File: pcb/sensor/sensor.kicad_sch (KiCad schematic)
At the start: 21 parts, among them J1 Conn_01x02_Pin, J2 Conn_01x02_Pin, J3 sig_in, J4 sig_out, J5 Conn_01x02_Pin, J6 Conn_01x02_Pin, Q1 S8550, U1 TJA1051T-3, U2 HX711

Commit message: update sensor
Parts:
- removed C1: 10uF, Capacitor_SMD:C_0603_1608Metric, symbol Device:C
- removed C4: 0.1uF, Capacitor_SMD:C_0603_1608Metric, symbol Device:C
- removed J1, J2: Conn_01x02_Pin, Connector_PinHeader_2.54mm:PinHeader_1x02_P2.54mm_Vertical, symbol Connector:Conn_01x02_Pin
- removed Q1: S8550, Package_TO_SOT_SMD:SOT-23, symbol Transistor_BJT:SS8550
- removed R1, R4: 20k, Resistor_SMD:R_0603_1608Metric, symbol Device:R_US
- added J7: Conn_02x02_Counter_Clockwise, Connector_PinHeader_2.54mm:PinHeader_2x02_P2.54mm_Vertical, symbol Connector_Generic:Conn_02x02_Odd_Even
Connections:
- net +3.3V: now also J7.1 (Pin_1); no longer U2.1 (VSUP)
- net +5V: now also U2.1 (VSUP), J7.2 (Pin_2)
- net GND: now also U2.4 (VFB), J7.3 (Pin_3), J7.4 (Pin_4)
- no-connect marks 3 -> 5
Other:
- moved on the sheet: C6

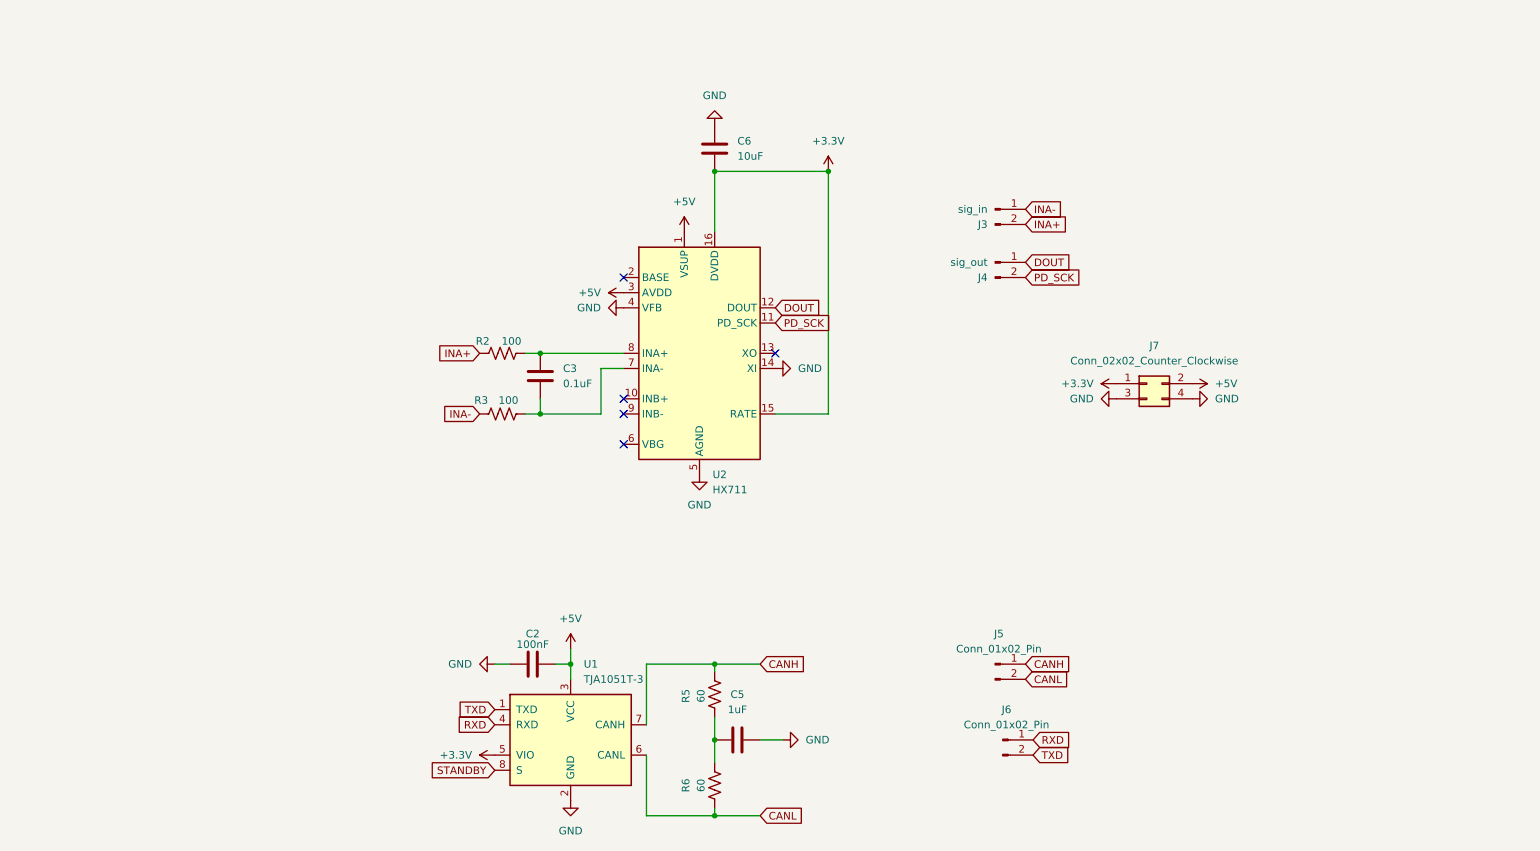
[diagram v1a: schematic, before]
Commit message: 更新kiacad sensor的原理图
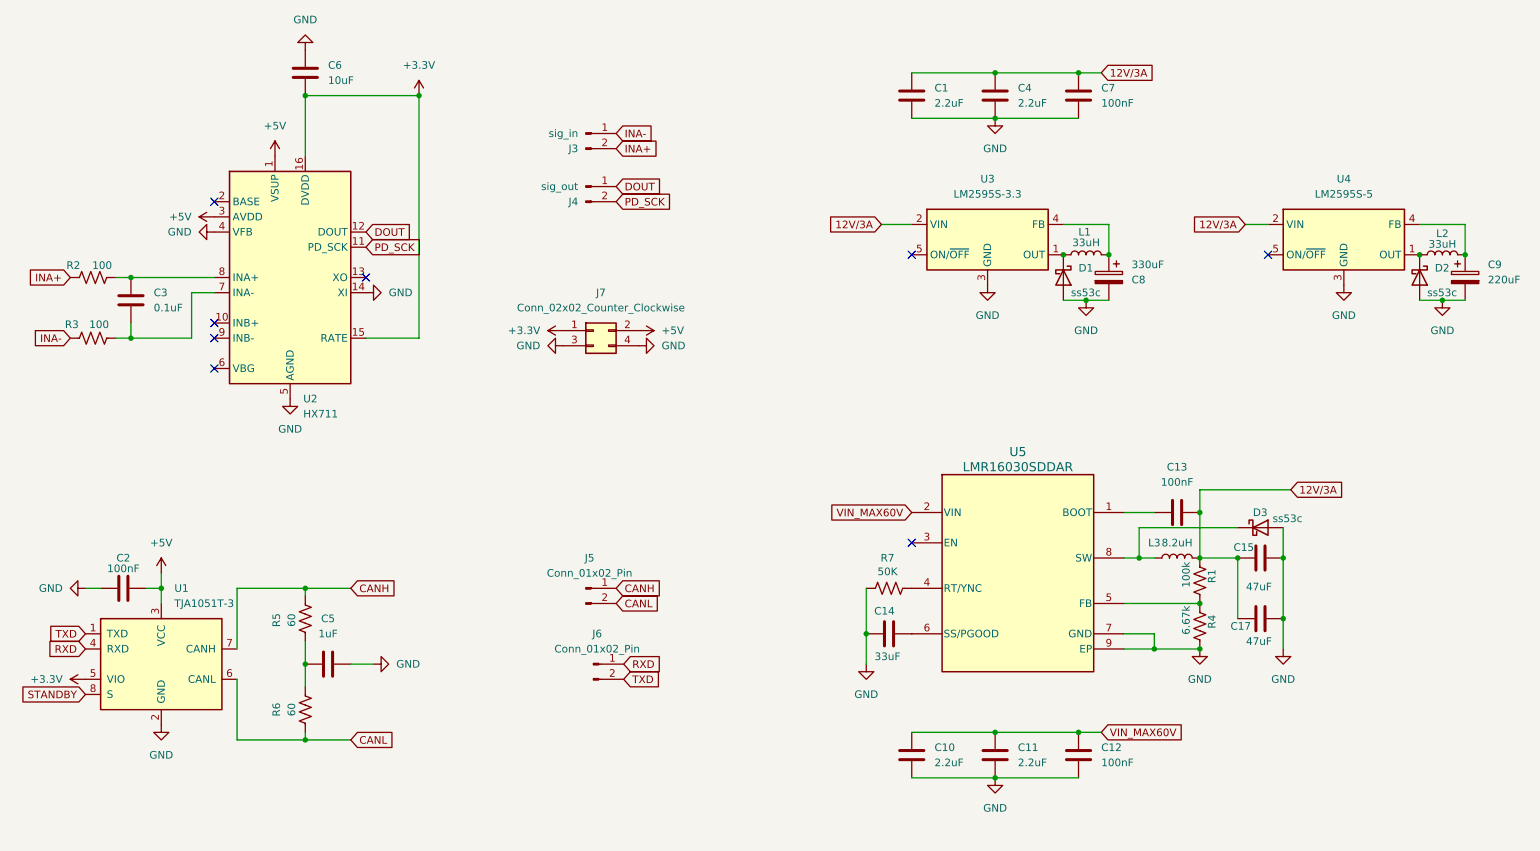
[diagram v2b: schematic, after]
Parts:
- added C1, C10, C11, C4: 2.2uF, symbol Device:C
- added C12, C13, C7: 100nF, Capacitor_SMD:C_0603_1608Metric, symbol Device:C
- added C14: 33uF, symbol Device:C
- added C15, C17: 47uF, symbol Device:C
- added C8: 330uF, symbol Device:C_Polarized
- added C9: 220uF, symbol Device:C_Polarized
- added D1, D2, D3: ss53c, symbol Device:D_Schottky
- added L1, L2: 33uH, symbol Device:L
- added L3: 8.2uH, symbol Device:L
- added R1: 100k, Resistor_SMD:R_0603_1608Metric, symbol Device:R_US
- added R4: 6.67k, Resistor_SMD:R_0603_1608Metric, symbol Device:R_US
- added R7: 50K, Resistor_SMD:R_0603_1608Metric, symbol Device:R_US
- added U3: LM2595S-3.3, Package_TO_SOT_SMD:TO-263-5_TabPin3, symbol Regulator_Switching:LM2595S-3.3
- added U4: LM2595S-5, Package_TO_SOT_SMD:TO-263-5_TabPin3, symbol Regulator_Switching:LM2595S-5
- added U5: LMR16030SDDAR, DDA0008E_N, symbol 2025-01-08_11-11-09:LMR16030SDDAR
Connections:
- net GND: now also C1.1, C10.1, C11.1, C12.1, C14.2, C15.2, C17.1, C4.1, C7.1, C8.2, C9.2, D1.2 (A), D2.2 (A), D3.2 (A), R4.2, R7.2, U3.3 (GND), U4.3 (GND), U5.7 (GND), U5.9 (EP)
- new net: C13.2, U5.1 (BOOT)
- new net: R7.1, U5.4 (RT/YNC)
- new net: R1.2, R4.1, U5.5 (FB)
- new net: C14.1, U5.6 (SS/PGOOD)
- new net: D3.1 (K), L3.1, U5.8 (SW)
- new net: D2.1 (K), L2.1, U4.1 (OUT)
- new net: C9.1, L2.2, U4.4 (FB)
- new net: D1.1 (K), L1.1, U3.1 (OUT)
- new net: C8.1, L1.2, U3.4 (FB)
- new net 12V/3A: C1.2, C13.1, C15.1, C17.2, C4.2, C7.2, L3.2, R1.1, U3.2 (VIN), U4.2 (VIN)
- new net VIN_MAX60V: C10.2, C11.2, C12.2, U5.2 (VIN)
- no-connect marks 5 -> 8
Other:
- moved on the sheet: C2, C3, C5, C6, J3, J4, J5, J6, J7, R2, R3, R5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
